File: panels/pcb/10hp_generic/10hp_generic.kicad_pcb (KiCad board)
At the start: 2 copper layers, 50 x 106.8 mm, 81 parts, among them J1 Conn_02x04_Odd_Even, J2 SWD, SW1 SW_Push, SW10 SW_Push, SW11 SW_Push, SW12 SW_Push, SW13 SW_Push, SW14 SW_Push, SW15 SW_Push, SW16 SW_Push, SW2 SW_Push, SW3 SW_Push, SW4 SW_Push, SW5 SW_Push, SW6 SW_Push, SW7 SW_Push, SW8 SW_Push, SW9 SW_Push, U1 STM32F072RBTx, U2 AMS1117-3.3

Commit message: PCB design for generic r3 (wip)
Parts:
- added C38: 20pF, Capacitor_SMD:C_0603_1608Metric, F.Cu at (77.6, 60.2)
- added C39: 20pF, Capacitor_SMD:C_0603_1608Metric, F.Cu at (73.8, 60.2)
- added C40: 100nF, Capacitor_SMD:C_0402_1005Metric, F.Cu at (80.1, 87.2)
- added C41: 100pF, Capacitor_SMD:C_0402_1005Metric, F.Cu at (68.5, 65.7)
- added R1: 10K, Resistor_SMD:R_0402_1005Metric, F.Cu at (69.6, 66.8)
- added U3: STM32F103C8Tx, Package_QFP:LQFP-48_7x7mm_P0.5mm, F.Cu at (75.5, 72.2)
- added Y1: 8MHz, riban:HC-49S, F.Cu at (75.5, 63.8)
- J1: value Conn_02x04_Odd_Even -> CAN_PWR; footprint Connector_IDC:IDC-Header_2x04_P2.54mm_Vertical -> Connector_IDC:IDC-Header_2x03_P2.54mm_Vertical
- U1: value STM32F072RBTx -> TJA1051T-3; footprint Package_QFP:LQFP-64_10x10mm_P0.5mm -> Package_SO:SOIC-8_3.9x4.9mm_P1.27mm
- moved C35 53.9 mm to (72.7, 115.1), turned to 180 degrees
- moved C34 53.9 mm to (72.6, 113.4), turned to 180 degrees
- moved C36 45.7 mm to (124.5, 116.1), turned to 0 degrees
- moved J2 44.5 mm to (120.4, 112.5)
- moved C32 41.3 mm to (76.2, 113.4), turned to 180 degrees
- moved C33 41.3 mm to (76.3, 115.1), turned to 180 degrees
- moved U2 41.2 mm to (74.0, 107.8), turned to 90 degrees
- moved C30 38.5 mm to (78.2, 78.0), turned to 180 degrees
- moved C31 36.6 mm to (78.2, 79.0), turned to 180 degrees
- moved C28 33.5 mm to (81.0, 67.5), turned to -90 degrees
- moved C29 32.4 mm to (82.7, 67.0), turned to -90 degrees
- moved C24 25.8 mm to (70.6, 76.6), turned to 180 degrees
- moved C25 24.2 mm to (70.6, 77.6), turned to 180 degrees
- moved C26 22.3 mm to (70.6, 78.7), turned to 180 degrees
- moved U1 20.2 mm to (75.5, 87.2), turned to 180 degrees
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- renumbered D3 to D1, D15 to D10, D14 to D11, D13 to D12, D12 to D13, D11 to D14, D10 to D15, D9 to D16, D4 to D2, D5 to D3, D6 to D4, D7 to D5, D8 to D6, D1 to D7, D2 to D8, D16 to D9
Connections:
- J1 pad 3: SCL -> CAN-H
- J1 pad 4: SDA -> CAN-L
- J1 pad 5: DETECT -> GND
- J1 pad 6: RESET -> GND
- U1 pad 1: unconnected-(U1-Pad1) -> Net-(U1-Pad1)
- U1 pad 2: unconnected-(U1-Pad2) -> +5V
- U1 pad 3: unconnected-(U1-Pad3) -> GND
- U1 pad 4: unconnected-(U1-Pad4) -> Net-(U1-Pad4)
- U1 pad 6: unconnected-(U1-Pad6) -> CAN-H
- U1 pad 7: RESET -> CAN-L
- U1 pad 8: POT2 -> GND
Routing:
- net VDD: track 282.8 -> 227.6 mm
- net SW8: track 31.8 -> 76.5 mm
- net SW4: track 49.1 -> 92.1 mm
- net SW7: track 24.3 -> 66.4 mm
- net SW3: track 39.4 -> 80.6 mm
- net POT8: track 76.2 -> 36.2 mm, vias 2 -> 1
- net SW6: track 25.3 -> 64.1 mm
- net SW5: track 34.6 -> 73.2 mm
- net SCL: track 37.2 -> 0.00 mm
- net SW2: track 40.0 -> 75.7 mm
- net POT7: track 71.2 -> 35.8 mm, vias 0 -> 1
- net POT2: track 30.9 -> 65.1 mm, vias 0 -> 1
- net SW1: track 51.7 -> 83.6 mm
- net SDA: track 31.4 -> 0.00 mm
- net GND: track 631.1 -> 605.4 mm, vias 5 -> 0
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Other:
- board text added: "Generic Modular Panel 10HP - Rev 3"
- board text added: "riban ltd © 2024"
- board text removed: "+5V"
- board text removed: "Generic Modular Panel 10HP - Rev 2"
- board text removed: "riban ltd © 2023"

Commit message: Rev 3 PCB routing done
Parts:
- moved C36 53.0 mm to (82.5, 83.7), turned to -90 degrees
- moved J2 48.7 mm to (80.8, 84.2), turned to 0 degrees
- moved D10 26.0 mm to (88.6, 88.4), turned to 0 degrees
- moved D14 26.0 mm to (62.6, 67.2), turned to 180 degrees
- moved D15 26.0 mm to (62.6, 88.4), turned to 180 degrees
- moved D16 26.0 mm to (62.6, 109.8), turned to 180 degrees
- moved D9 26.0 mm to (88.6, 109.8), turned to 0 degrees
- moved D11 25.9 mm to (88.5, 67.2), turned to 0 degrees
- moved D4 25.1 mm to (69.5, 140.7)
- moved D7 25.1 mm to (94.7, 127.3)
- moved D3 25.1 mm to (56.9, 140.7)
- moved D8 25.1 mm to (82.1, 127.3)
- moved D5 18.3 mm to (82.1, 140.7), turned to 180 degrees
- moved D6 18.3 mm to (94.7, 140.7), turned to 180 degrees
- moved D1 18.3 mm to (69.5, 127.3), turned to 0 degrees
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- renumbered D13 to D12, D12 to D13
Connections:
- D1 pad 2: Net-(D2-Pad4) (its old number) -> WS2812
- D10 pad 2: Net-(D14-Pad4) -> Net-(D10-Pad2)
- D10 pad 4: Net-(D15-Pad4) -> Net-(D10-Pad4)
- D11 pad 2: Net-(D13-Pad4) -> Net-(D10-Pad4)
- D11 pad 4: Net-(D14-Pad4) -> Net-(D11-Pad4)
- D14 pad 2: Net-(D10-Pad4) -> Net-(D13-Pad4)
- D14 pad 4: Net-(D11-Pad4) -> Net-(D14-Pad4)
- D15 pad 2: Net-(D10-Pad2) -> Net-(D14-Pad4)
- D15 pad 4: Net-(D10-Pad4) -> Net-(D15-Pad4)
- D16 pad 2: Net-(D8-Pad4) -> Net-(D15-Pad4)
- D16 pad 4: Net-(D10-Pad2) -> unconnected-(D16-Pad4)
- D6 pad 4: Net-(D8-Pad4) -> Net-(D6-Pad4)
- D7 pad 2: WS2812 -> Net-(D6-Pad4)
- D8 pad 4: Net-(D2-Pad4) (its old number) -> Net-(D8-Pad4)
- D9 pad 2: Net-(D15-Pad4) -> Net-(D8-Pad4)
- D9 pad 4: unconnected-(D16-Pad4) -> Net-(D10-Pad2)
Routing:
- net GND: track 605.4 -> 686.9 mm, vias 0 -> 8
- net WS2812: track 5.91 -> 67.6 mm, vias 2 -> 0
- net VDD: track 227.6 -> 272.5 mm, vias 2 -> 4
- net Net-(D6-Pad4): track 0.00 -> 19.7 mm
- net Net-(D2-Pad4) (its old number): track 17.3 -> 0.00 mm
- net +5V: track 436.0 -> 449.8 mm, vias 0 -> 2
- net SWDIO: track 0.00 -> 8.42 mm, vias 0 -> 1
- net Net-(D2-Pad4): track 11.4 -> 19.6 mm
- net Net-(D4-Pad4): track 18.7 -> 11.4 mm
- net SWCLK: track 0.00 -> 7.35 mm
- net POT3: track 45.9 -> 38.9 mm
- net SW1: track 83.6 -> 89.3 mm
- net POT5: track 26.1 -> 20.7 mm
- net POT7: track 35.8 -> 30.4 mm
- net SW5: track 73.2 -> 78.1 mm
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- added copper zone on F.Cu, net GND
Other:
- board text added: "+3V"
- board text added: "CH"
- board text added: "CL"
- board text removed: "1W"
- board text removed: "3.3V"
- board text removed: "RESET"
- board text removed: "SCL"
- board text removed: "SDA"

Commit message: Rev 3 boards complete - probably
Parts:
- added J3: I2C, Connector_PinHeader_2.54mm:PinHeader_1x04_P2.54mm_Vertical, F.Cu at (98.3, 75.4)
- C38, C39: value 20pF -> 22pF
- D1, D10, D11, D12, D13, D14, D15, D16, D2, D3, D4, D5, D6, D7, D8, D9: footprint WS2812:XL-2121RGBC-WS2812B -> riban:LED_XL-1615RGBC-WS2812B
- SW1, SW10, SW11, SW12, SW13, SW14, SW15, SW16, SW2, SW3, SW4, SW5, SW6, SW7, SW8, SW9: footprint Button_Switch_THT:SW_PUSH_6mm_H4.3mm -> riban:SW_PUSH_6mm_H4.3mm
- moved C36 34.3 mm to (75.6, 50.1), turned to 180 degrees
- moved J2 33.4 mm to (71.9, 52.0), turned to -90 degrees
- moved RV2 10.4 mm to (90.3, 114.5)
- moved RV1 9.75 mm to (62.3, 114.5)
- moved RV4 9.49 mm to (90.3, 94.2)
- moved RV3 8.81 mm to (62.3, 94.2)
- moved RV6 8.62 mm to (90.3, 73.9)
- moved C2 7.93 mm to (89.1, 123.8), turned to 0 degrees
- moved RV5 7.87 mm to (62.3, 73.9)
- moved RV8 7.78 mm to (90.3, 53.6)
- moved RV7 6.94 mm to (62.3, 53.6)
- moved SW9 5.60 mm to (62.3, 114.5)
- moved SW11 4.71 mm to (62.3, 94.2)
- moved SW1 4.55 mm to (57.2, 145.0)
- moved SW2 4.47 mm to (70.0, 145.0)
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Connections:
- D1 pad 1: GND -> Net-(D1-Pad1)
- D1 pad 2: WS2812 -> +5V
- D1 pad 3: +5V -> GND
- D1 pad 4: Net-(D1-Pad4) -> WS2812
- D10 pad 1: GND -> Net-(D10-Pad1)
- D10 pad 2: Net-(D10-Pad2) -> +5V
- D10 pad 3: +5V -> GND
- D11 pad 1: GND -> Net-(D11-Pad1)
- D11 pad 2: Net-(D10-Pad4) -> +5V
- D11 pad 3: +5V -> GND
- D11 pad 4: Net-(D11-Pad4) -> Net-(D10-Pad1)
- D12 pad 1: GND -> Net-(D12-Pad1)
- D12 pad 2: Net-(D11-Pad4) -> +5V
- D12 pad 3: +5V -> GND
- D12 pad 4: Net-(D12-Pad4) -> Net-(D11-Pad1)
- D13 pad 1: GND -> Net-(D13-Pad1)
- D13 pad 2: Net-(D12-Pad4) -> +5V
- D13 pad 3: +5V -> GND
- D13 pad 4: Net-(D13-Pad4) -> Net-(D12-Pad1)
- D14 pad 1: GND -> Net-(D14-Pad1)
- D14 pad 2: Net-(D13-Pad4) -> +5V
- D14 pad 3: +5V -> GND
- D14 pad 4: Net-(D14-Pad4) -> Net-(D13-Pad1)
- D15 pad 1: GND -> Net-(D15-Pad1)
- D15 pad 2: Net-(D14-Pad4) -> +5V
- D15 pad 3: +5V -> GND
- D15 pad 4: Net-(D15-Pad4) -> Net-(D14-Pad1)
- D16 pad 1: GND -> unconnected-(D16-Pad1)
- D16 pad 2: Net-(D15-Pad4) -> +5V
- D16 pad 3: +5V -> GND
- D16 pad 4: unconnected-(D16-Pad4) -> Net-(D15-Pad1)
- D2 pad 1: GND -> Net-(D2-Pad1)
- D2 pad 2: Net-(D1-Pad4) -> +5V
- D2 pad 3: +5V -> GND
- D2 pad 4: Net-(D2-Pad4) -> Net-(D1-Pad1)
- D3 pad 1: GND -> Net-(D3-Pad1)
- D3 pad 2: Net-(D2-Pad4) -> +5V
- D3 pad 3: +5V -> GND
- D3 pad 4: Net-(D3-Pad4) -> Net-(D2-Pad1)
- D4 pad 1: GND -> Net-(D4-Pad1)
- D4 pad 2: Net-(D3-Pad4) -> +5V
- D4 pad 3: +5V -> GND
- D4 pad 4: Net-(D4-Pad4) -> Net-(D3-Pad1)
- D5 pad 1: GND -> Net-(D5-Pad1)
- D5 pad 2: Net-(D4-Pad4) -> +5V
- D5 pad 3: +5V -> GND
- D5 pad 4: Net-(D5-Pad4) -> Net-(D4-Pad1)
- D6 pad 1: GND -> Net-(D6-Pad1)
- D6 pad 2: Net-(D5-Pad4) -> +5V
- D6 pad 3: +5V -> GND
- D6 pad 4: Net-(D6-Pad4) -> Net-(D5-Pad1)
- D7 pad 1: GND -> Net-(D7-Pad1)
- D7 pad 2: Net-(D6-Pad4) -> +5V
- D7 pad 3: +5V -> GND
- D7 pad 4: Net-(D7-Pad4) -> Net-(D6-Pad1)
- D8 pad 1: GND -> Net-(D8-Pad1)
- D8 pad 2: Net-(D7-Pad4) -> +5V
- D8 pad 3: +5V -> GND
- D8 pad 4: Net-(D8-Pad4) -> Net-(D7-Pad1)
- D9 pad 1: GND -> Net-(D10-Pad4)
- D9 pad 2: Net-(D8-Pad4) -> +5V
- D9 pad 3: +5V -> GND
- D9 pad 4: Net-(D10-Pad2) -> Net-(D8-Pad1)
- J2 pad 2: SWCLK -> SWDIO
- J2 pad 3: SWDIO -> SWCLK
- U3 pad 42: SDA -> SCL
- U3 pad 43: SCL -> SDA
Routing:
- net VDD: track 272.5 -> 360.0 mm, vias 4 -> 0
- net Net-(D8-Pad1): track 0.00 -> 37.3 mm
- net Net-(D8-Pad4): track 34.7 -> 0.00 mm
- net Net-(D10-Pad1): track 0.00 -> 32.9 mm
- net Net-(D11-Pad1): track 0.00 -> 31.7 mm
- net Net-(D11-Pad4): track 30.6 -> 0.00 mm
- net Net-(D10-Pad2): track 30.2 -> 0.00 mm
- net Net-(D13-Pad4): track 30.2 -> 0.00 mm
- net Net-(D13-Pad1): track 0.00 -> 29.4 mm
- net GND: track 686.9 -> 657.7 mm, vias 8 -> 3
- net Net-(D12-Pad1): track 0.00 -> 27.0 mm
- net Net-(D14-Pad1): track 0.00 -> 26.2 mm
- net Net-(D15-Pad1): track 0.00 -> 26.0 mm
- net Net-(D12-Pad4): track 24.7 -> 0.00 mm
- net +5V: track 449.8 -> 474.2 mm
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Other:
- board size 50 x 106.8 mm -> 48.8 x 106 mm
- rule pad_to_mask_clearance: 0 -> 0.05
- board text added: "3.3V"
- board text added: "CLK"
- board text added: "DIO"
- board text added: "SCL"
- board text added: "SDA"
- board text removed: "+3V"
- board text removed: "SWCLK"
- board text removed: "SWDIO"

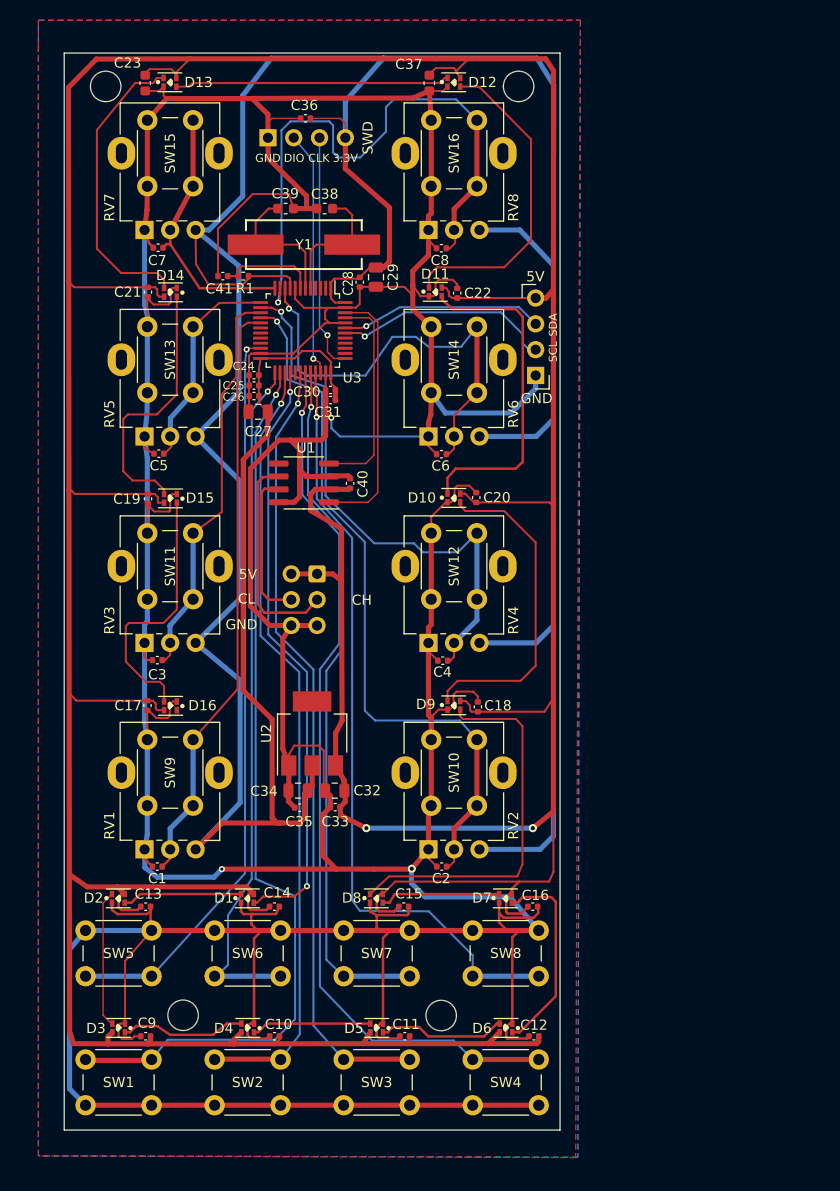
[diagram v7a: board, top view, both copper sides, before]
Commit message: R3 PCB and front panel
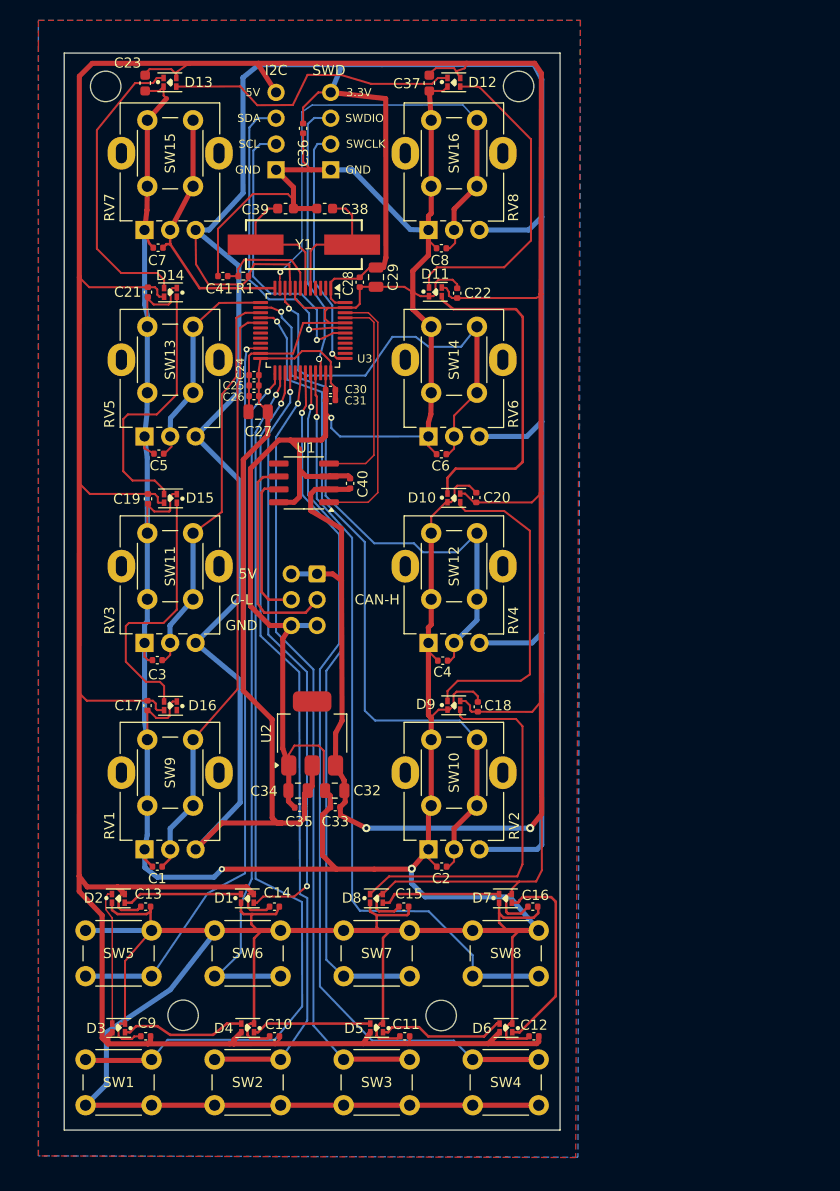
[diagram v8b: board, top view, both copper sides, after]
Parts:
- J3: moved to B.Cu
- moved J3 32.6 mm to (72.8, 55.2), turned to 0 degrees
- moved J2 6.94 mm to (78.1, 55.2), turned to 0 degrees
- moved C36 1.01 mm to (75.4, 51.1), turned to -90 degrees
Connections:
- J2 pad 2: SWDIO -> SWCLK
- J2 pad 3: SWCLK -> SWDIO
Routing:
- net GND: track 657.7 -> 630.1 mm
- net +5V: track 474.2 -> 462.9 mm
- net SDA: track 19.9 -> 30.5 mm
- net POT8: track 59.9 -> 50.5 mm
- net SCL: track 21.6 -> 28.4 mm
- net SWDIO: track 24.2 -> 27.8 mm
- net VDD: track 360.0 -> 356.4 mm
- net Net-(D12-DOUT): track 27.0 -> 29.7 mm
- net Net-(U3-NRST): track 9.75 -> 10.5 mm
- net SWCLK: track 23.4 -> 24.1 mm
- net SW2: track 77.0 -> 77.6 mm
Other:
- board text added: "C-L"
- board text added: "CAN-H"
- board text added: "CAN-L"
- board text added: "I2C"
- board text added: "SWCLK"
- board text added: "SWD"
- board text added: "SWDIO"
- board text removed: "CH"
- board text removed: "CL"
- board text removed: "CLK"
- board text removed: "DIO"
